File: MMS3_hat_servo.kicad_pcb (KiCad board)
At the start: 2 copper layers, 100 x 50 mm, 59 parts, among them J1 Chainbus in, J10 Conn_01x03, J2 Chainbus Out, J3 Conn_01x04_Pin, J4 AMASS XT60 Male, J5 AMASS XT60 Female, J7 Conn_01x03, J8 Conn_01x03, J9 Conn_01x03, Q1 2N7002K, Q2 2N7002K, U1 PCA9685PW,118, U2 M24C64, U3 SN74CB3Q3245PWR, U4 AMS1117

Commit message: PCB design
Adjustments
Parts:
- moved C2 40.4 mm to (129.8, 104.6), turned to 0 degrees
- moved C29 32.7 mm to (121.2, 128.8), turned to 180 degrees
- moved C30 13.9 mm to (149.6, 108.5)
- moved G*** 4.65 mm to (166.9, 124.0)
- moved J10 2.26 mm to (123.7, 132.4)
- moved J9 1.51 mm to (136.8, 132.4)
- moved J8 0.75 mm to (149.9, 132.4)
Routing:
- net GND: track 246.4 -> 60.3 mm, vias 40 -> 33
- net /Power Connector/VIN_BRD: track 113.0 -> 30.3 mm, vias 0 -> 1
- net +3V3: track 116.1 -> 118.8 mm
- net /Servo controller/S1: track 45.9 -> 48.1 mm
- net /Bus_switch/Chainbus.SDA: track 74.5 -> 72.3 mm
- net +5V: track 107.7 -> 108.5 mm
- net /Servo controller/A3: track 10.8 -> 10.1 mm
- net /Bus_switch/SEL1: track 78.7 -> 78.0 mm
- net /Servo controller/S2: track 33.7 -> 34.3 mm
- net BRD_VIN: track 22.2 -> 21.9 mm, vias 6 -> 7
- added copper zone on B.Cu, net /Power Connector/VIN_BRD
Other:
- board text added: "Hat servo controller version 1.0 by Szymon Filip"
- board text added: "OFF LED"
- board text added: "ON LED"
- board text added: "PINOUT SERVO [Vcc S GND]^"
- board text added: "SERVO 1"
- board text added: "SERVO 2"
- board text added: "SERVO 3"
- board text added: "SERVO 4"
- board text removed: "PINOUT SERVO ^[GND S Vcc]"

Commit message: Revieved by Wojtek
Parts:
- removed D4: SS510C, SS510C:SMC_L7.1-W6.2-LS8.1-RD
- added D1: M7, PCM_JLCPCB:D_SMA, F.Cu at (96.5, 99.5)
- moved C29 1.57 mm to (120.2, 127.5), turned to 90 degrees
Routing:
- net BRD_VIN: track 21.9 -> 33.3 mm, vias 7 -> 9
- net GND: track 60.3 -> 56.7 mm, vias 33 -> 78
- net /Servo controller/S2: track 34.3 -> 34.9 mm
- net /Power Connector/VIN_BRD: track 30.3 -> 30.1 mm, vias 1 -> 0
- net /Bus_switch/Chainbus.SCL: vias 2 -> 1
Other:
- board text added: "S15 LED"
- board text added: "S16 LED"
- board text removed: "OFF LED"
- board text removed: "ON LED"

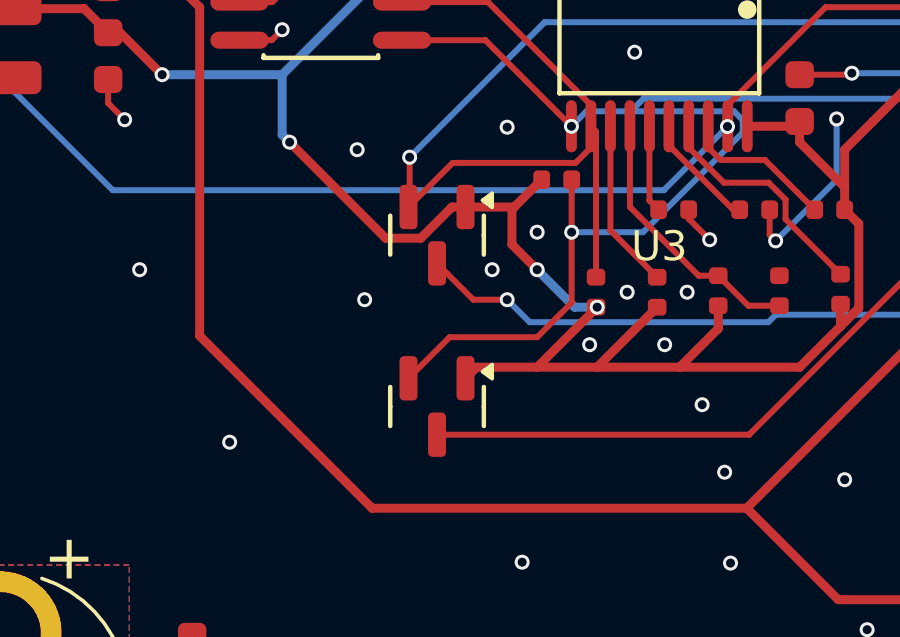
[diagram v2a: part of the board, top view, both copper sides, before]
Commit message: change mosfets to basic assembly
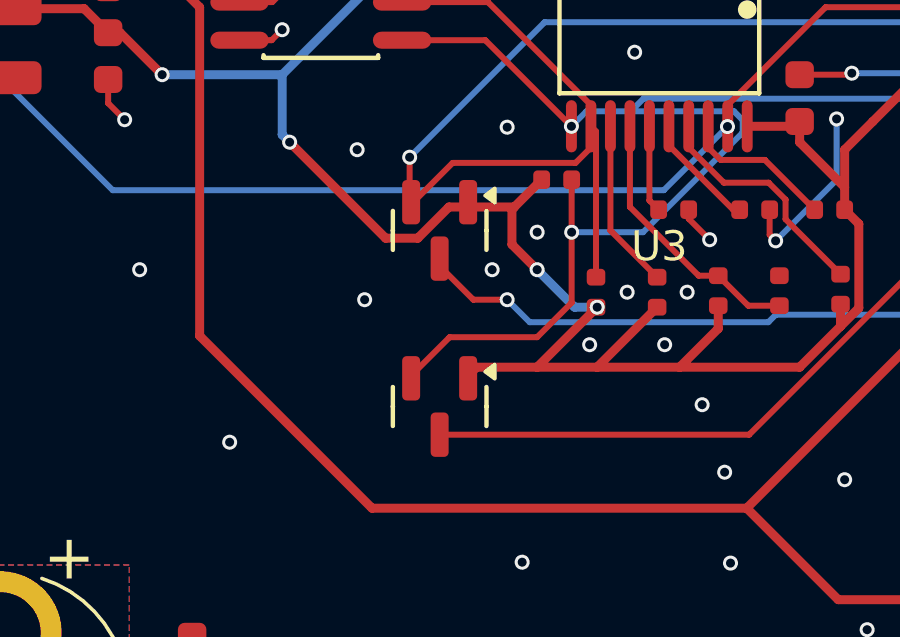
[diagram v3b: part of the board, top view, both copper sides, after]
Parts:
- removed Q1, Q2: 2N7002K, PCM_JLCPCB:Q_SOT-23
- added Q4: AO3400A, PCM_JLCPCB:Q_SOT-23, F.Cu at (128.5, 113.2)
- added Q5: AO3400A, PCM_JLCPCB:Q_SOT-23, F.Cu at (128.5, 119.1)
